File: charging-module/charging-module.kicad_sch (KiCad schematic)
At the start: 12 parts, among them J1 Bat, U1 MCP73833-xxx-UN

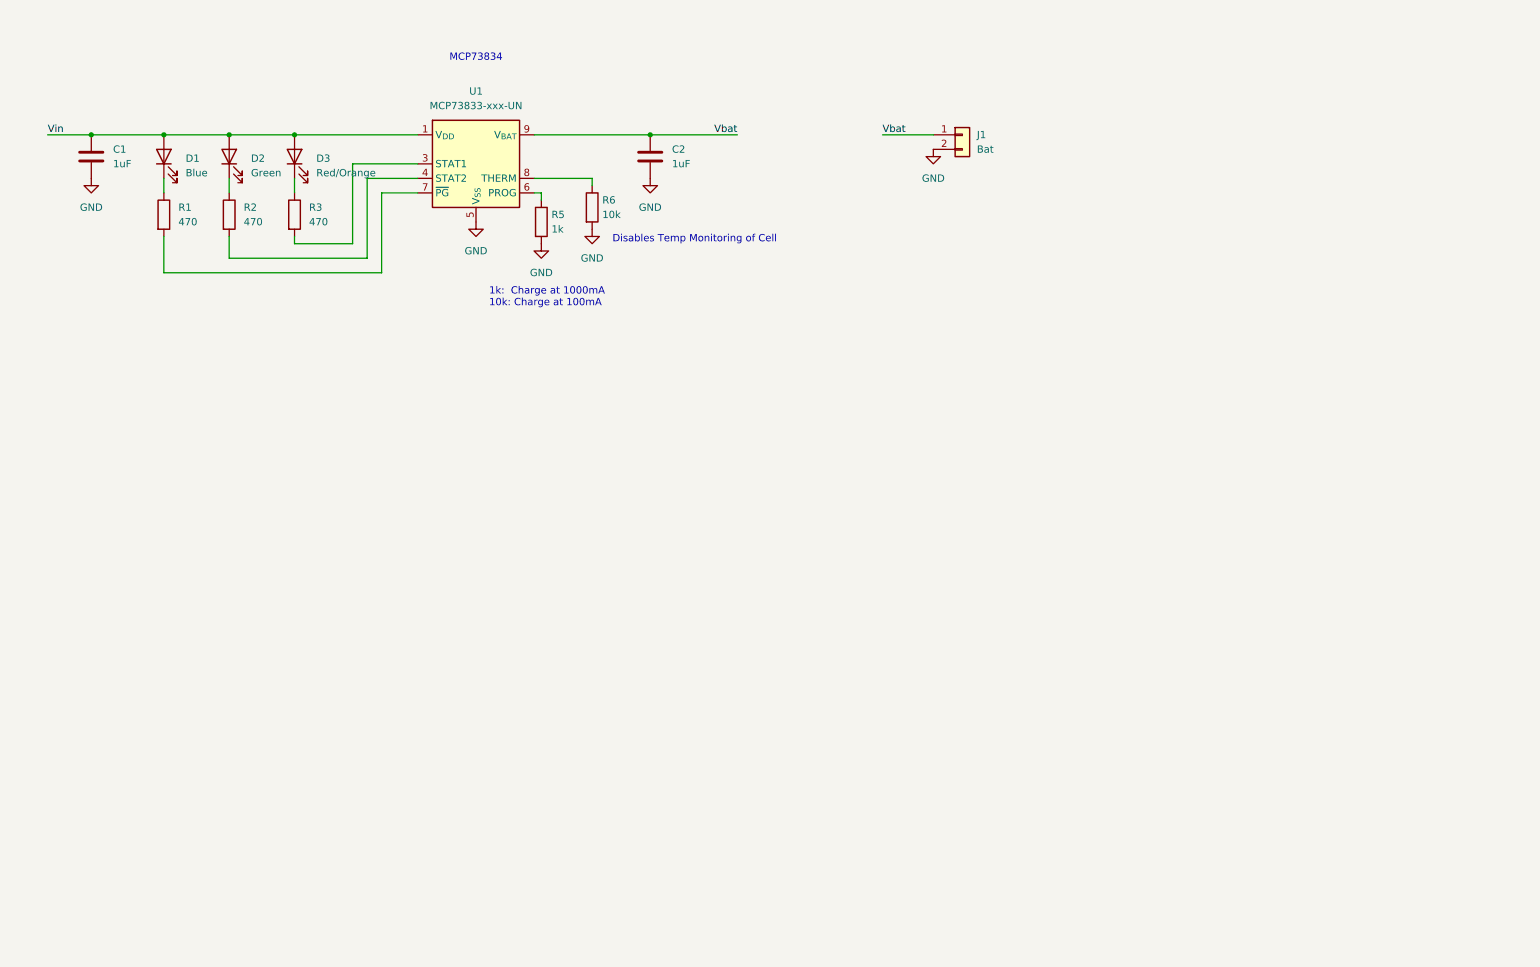
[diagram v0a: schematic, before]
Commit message: MCP73871 schematic
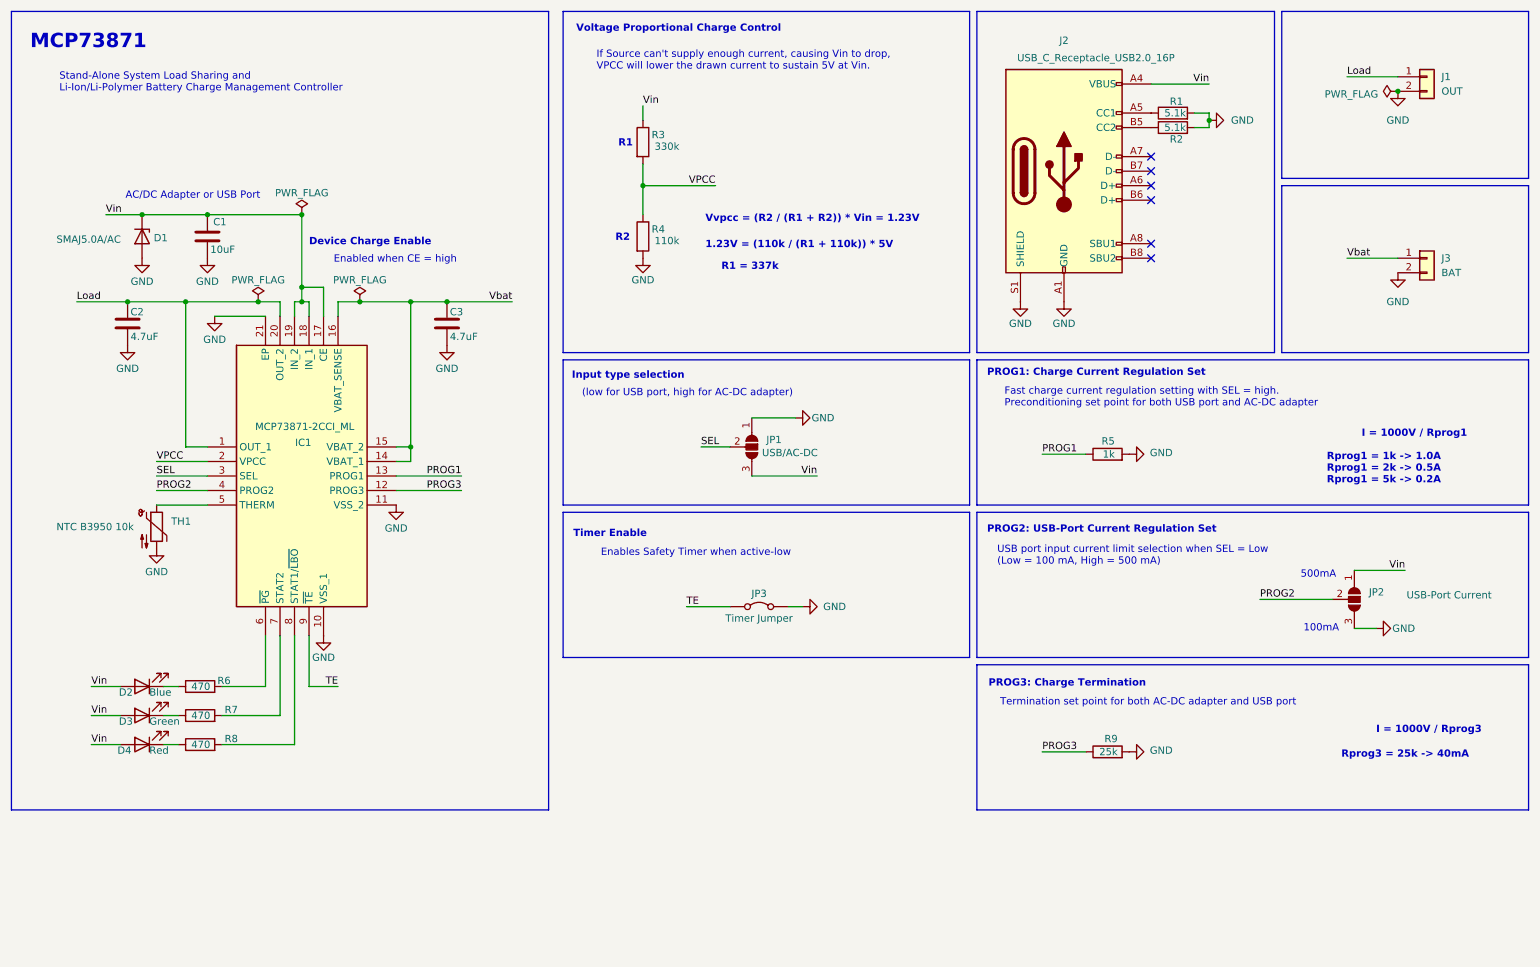
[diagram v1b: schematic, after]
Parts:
- removed D1: Blue, symbol Device:LED
- removed U1: MCP73833-xxx-UN, Package_SO:MSOP-10_3x3mm_P0.5mm, symbol Battery_Management:MCP73833-xxx-UN
- added C3: 4.7uF, symbol Device:C
- added D1: SMAJ5.0A/AC, symbol Device:D_Zener
- added D4: Red, symbol Device:LED
- added IC1: MCP73871-2CCI_ML, MCP73871-2CCI_ML:QFN50P400X400X100-21N-D, symbol MCP73871-2CCI_ML:MCP73871-2CCI_ML
- added J1: OUT, Connector_JST:JST_XH_S2B-XH-A_1x02_P2.50mm_Horizontal, symbol Connector_Generic:Conn_01x02
- added J2: USB_C_Receptacle_USB2.0_16P, Connector_USB:USB_C_Receptacle_HRO_TYPE-C-31-M-12, symbol Connector:USB_C_Receptacle_USB2.0_16P
- added JP1: USB/AC-DC, Connector_PinHeader_2.54mm:PinHeader_1x03_P2.54mm_Horizontal, symbol Jumper:SolderJumper_3_Open
- added JP2: USB-Port Current, Jumper:SolderJumper-3_P1.3mm_Bridged12_RoundedPad1.0x1.5mm_NumberLabels, symbol Jumper:SolderJumper_3_Open
- added JP3: Timer Jumper, Jumper:SolderJumper-2_P1.3mm_Bridged_RoundedPad1.0x1.5mm, symbol Jumper:Jumper_2_Bridged
- added R4: 110k, symbol Device:R
- added R7, R8: 470, symbol Device:R
- added R9: 25k, symbol Device:R
- added TH1: NTC B3950 10k, Connector_PinHeader_1.00mm:PinHeader_1x02_P1.00mm_Vertical, symbol Device:Thermistor_NTC
- C1: value 1uF -> 10uF
- C2: value 1uF -> 4.7uF
- D2: value Green -> Blue
- D3: value Red/Orange -> Green
- J3: renamed from J1; value Bat -> BAT; footprint (none) -> Connector_JST:JST_XH_S2B-XH-A_1x02_P2.50mm_Horizontal
- R1, R2: value 470 -> 5.1k
- R3: value 470 -> 330k
- R6: value 10k -> 470
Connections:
- net GND: now also R1.2, R2.2, C3.2, D1.2 (A), IC1.10 (VSS_1), IC1.11 (VSS_2), IC1.21 (EP), J1.2 (Pin_2), J2.A1 (GND), J2.A12 (GND), J2.B1 (GND), J2.B12 (GND), J2.S1 (SHIELD), JP1.1 (A), JP2.3 (B), JP3.2 (B), R4.2, R9.2, TH1.2; no longer R6.2
- net Vbat: now also C3.1, IC1.14 (VBAT_1), IC1.15 (VBAT_2), IC1.16 (VBAT_SENSE); no longer C2.1
- net Vin: now also R3.1, D1.1 (K), D4.2 (A), IC1.17 (CE), IC1.18 (IN_1), IC1.19 (IN_2), J2.A4 (VBUS), J2.A9 (VBUS), J2.B4 (VBUS), J2.B9 (VBUS), JP1.3 (B), JP2.1 (A)
- net at R1.1: now also J2.A5 (CC1)
- net at D2.1 (K): now also R6.1; no longer R2.1
- net PROG1: now reaches R5.1
- net PROG1: now also IC1.13 (PROG1)
- net at D3.1 (K): now also R7.1; no longer R3.1
- net VPCC: now reaches R3.2
- net VPCC: now also IC1.2 (VPCC), R4.1
- new net: IC1.5 (THERM), TH1.1
- new net: IC1.7 (STAT2), R7.2
- new net: IC1.6 (~{PG}), R6.2
- new net: IC1.8 (STAT1/~{LBO}), R8.2
- new net: J2.B5 (CC2), R2.1
- new net: D4.1 (K), R8.1
- new net Load: C2.1, IC1.1 (OUT_1), IC1.20 (OUT_2), J1.1 (Pin_1)
- new net PROG2: IC1.4 (PROG2), JP2.2 (C)
- new net PROG3: IC1.12 (PROG3), R9.1
- new net SEL: IC1.3 (SEL), JP1.2 (C)
- new net TE: IC1.9 (~{TE}), JP3.1 (A)
- no-connect marks 0 -> 6
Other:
- note added: "(low for USB port, high for AC-DC adapter)"
- note added: "1.23V = (110k / (R1 + 110k)) * 5V"
- note added: "100mA"
- note added: "500mA"
- note added: "AC/DC Adapter or USB Port"
- note added: "Device Charge Enable"
- note added: "Enabled when CE = high"
- note added: "Enables Safety Timer when active-low"
- note added: "Fast charge current regulation setting with SEL = high. Preconditioning set point for both USB port and AC-DC adapter"
- note added: "I = 1000V / Rprog1"
- note added: "I = 1000V / Rprog3"
- note added: "If Source can't supply enough current, causing Vin to drop, VPCC will lower the drawn current to sustain 5V at Vin."
- note added: "Input type selection"
- note added: "MCP73871"
- note added: "PROG1: Charge Current Regulation Set"
- note added: "PROG2: USB-Port Current Regulation Set"
- note added: "PROG3: Charge Termination"
- note added: "R1"
- note added: "R1 = 337k"
- note added: "R2"
- note added: "Rprog1 = 1k -> 1.0A"
- note added: "Rprog1 = 2k -> 0.5A"
- note added: "Rprog1 = 5k -> 0.2A"
- note added: "Rprog3 = 25k -> 40mA"
- note added: "Stand-Alone System Load Sharing and Li-Ion/Li-Polymer Battery Charge Management Controller"
- note added: "Termination set point for both AC-DC adapter and USB port"
- note added: "Timer Enable"
- note added: "USB port input current limit selection when SEL = Low (Low = 100 mA, High = 500 mA)"
- note added: "Voltage Proportional Charge Control"
- note added: "Vvpcc = (R2 / (R1 + R2)) * Vin = 1.23V"
- note removed: "1k: Charge at 1000mA 10k: Charge at 100mA"
- note removed: "Disables Temp Monitoring of Cell"
- note removed: "MCP73834"
- moved on the sheet: J3

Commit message: removed overvoltage diode
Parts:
- removed D1: SMAJ5.0A/AC, symbol Device:D_Zener
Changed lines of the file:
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@@
 	)
 	(junction
-		(at 40.64 49.53)
-		(diameter 0)
-		(color 0 0 0 0)
-	)
-	(junction
 		(at 38.1 64.77)
 		(diameter 0)
@@
 	(wire
 		(pts
-			(xy 40.64 49.53) (xy 52.07 49.53)
-		)
-		(stroke
-			(width 0)
-			(type default)
-		)
-	)
-	(wire
-		(pts
 			(xy 62.23 132.08) (xy 62.23 123.19)
 		)
@@
 	(wire
 		(pts
-			(xy 34.29 49.53) (xy 40.64 49.53)
+			(xy 34.29 49.53) (xy 52.07 49.53)
 		)
 		(stroke
@@
 	(symbol
 		(lib_id "power:GND")
-		(at 40.64 57.15 0)
-		(unit 1)
-		(exclude_from_sim no)
-		(in_bom yes)
-		(on_board yes)
-		(dnp no)
-		(property "Reference" "#PWR03"
-			(at 40.64 63.5 0)
-			(effects
-				(font
-					(size 1.27 1.27)
-				)
-				(hide yes)
-			)
-		)
-		(property "Value" "GND"
-			(at 40.64 61.214 0)
-			(effects
-				(font
-					(size 1.27 1.27)
-				)
-			)
-		)
-		(property "Footprint" ""
-			(at 40.64 57.15 0)
-			(effects
-				(font
-					(size 1.27 1.27)
-				)
-				(hide yes)
-			)
-		)
-		(property "Datasheet" ""
-			(at 40.64 57.15 0)
-			(effects
-				(font
-					(size 1.27 1.27)
-				)
-				(hide yes)
-			)
-		)
-		(property "Description" "Power symbol creates a global label with name \"GND\" , ground"
-			(at 40.64 57.15 0)
-			(effects
-				(font
-					(size 1.27 1.27)
-				)
-				(hide yes)
-			)
-		)
-		(pin "1"
-		)
-		(instances
-			(project "charging-module"
-				(path "/81b77902-7571-4357-bdb3-0a0c14837efb"
-					(reference "#PWR03")
-					(unit 1)
-				)
-			)
-		)
-	)
-	(symbol
-		(lib_id "power:GND")
 		(at 53.34 67.31 0)
 		(unit 1)
@@
 					(unit 1)
 				)
-			)
-		)
-	)
-	(symbol
-		(lib_id "Device:D_Zener")
-		(at 40.64 53.34 270)
-		(unit 1)
-		(exclude_from_sim no)
-		(in_bom yes)
-		(on_board yes)
-		(dnp no)
-		(property "Reference" "D1"
-			(at 42.672 53.594 90)
-			(effects
-				(font
-					(size 1.27 1.27)
-				)
-				(justify left)
-			)
-		)
-		(property "Value" "SMAJ5.0A/AC"
-			(at 25.654 53.848 90)
-			(effects
-				(font
-					(size 1.27 1.27)
-				)
-				(justify left)
-			)
-		)
-		(property "Footprint" ""
-			(at 40.64 53.34 0)
-			(effects
-				(font
-					(size 1.27 1.27)
-				)
-				(hide yes)
-			)
-		)
-		(property "Datasheet" "~"
-			(at 40.64 53.34 0)
-			(effects
-				(font
-					(size 1.27 1.27)
-				)
-				(hide yes)
-			)
-		)
-		(property "Description" "Zener diode"
-			(at 40.64 53.34 0)
-			(effects
-				(font
-					(size 1.27 1.27)
-				)
-				(hide yes)
-			)
-		)
-		(pin "2"
-		)
-		(pin "1"
-		)
-		(instances
-			(project ""
-				(path "/81b77902-7571-4357-bdb3-0a0c14837efb"
-					(reference "D1")
-					(unit 1)
-				)

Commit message: assigned footprints
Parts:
- C1, C2, C3: footprint (none) -> Capacitor_SMD:C_0805_2012Metric_Pad1.18x1.45mm_HandSolder
- D2, D3, D4: footprint (none) -> LED_SMD:LED_0805_2012Metric_Pad1.15x1.40mm_HandSolder
- R1, R2, R3, R4, R5, R6, R7, R8, R9: footprint (none) -> Resistor_SMD:R_0805_2012Metric_Pad1.20x1.40mm_HandSolder
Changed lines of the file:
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@@
 			)
 		)
-		(property "Footprint" ""
+		(property "Footprint" "Resistor_SMD:R_0805_2012Metric_Pad1.20x1.40mm_HandSolder"
 			(at 50.8 138.938 90)
 			(effects
@@
 			)
 		)
-		(property "Footprint" ""
+		(property "Footprint" "Capacitor_SMD:C_0805_2012Metric_Pad1.18x1.45mm_HandSolder"
 			(at 94.9452 72.39 0)
 			(effects
@@
 			)
 		)
-		(property "Footprint" ""
+		(property "Footprint" "Capacitor_SMD:C_0805_2012Metric_Pad1.18x1.45mm_HandSolder"
 			(at 53.0352 57.15 0)
 			(effects
@@
 			)
 		)
-		(property "Footprint" ""
+		(property "Footprint" "LED_SMD:LED_0805_2012Metric_Pad1.15x1.40mm_HandSolder"
 			(at 40.64 132.08 0)
 			(effects
@@
 			)
 		)
-		(property "Footprint" ""
+		(property "Footprint" "LED_SMD:LED_0805_2012Metric_Pad1.15x1.40mm_HandSolder"
 			(at 40.64 137.16 0)
 			(effects
@@
 			)
 		)
-		(property "Footprint" ""
+		(property "Footprint" "Resistor_SMD:R_0805_2012Metric_Pad1.20x1.40mm_HandSolder"
 			(at 50.8 144.018 90)
 			(effects
@@
 			)
 		)
-		(property "Footprint" ""
+		(property "Footprint" "Capacitor_SMD:C_0805_2012Metric_Pad1.18x1.45mm_HandSolder"
 			(at 39.0652 72.39 0)
 			(effects
@@
 			)
 		)
-		(property "Footprint" ""
+		(property "Footprint" "Resistor_SMD:R_0805_2012Metric_Pad1.20x1.40mm_HandSolder"
 			(at 126.492 36.83 90)
 			(effects
@@
 			)
 		)
-		(property "Footprint" ""
+		(property "Footprint" "Resistor_SMD:R_0805_2012Metric_Pad1.20x1.40mm_HandSolder"
 			(at 220.98 36.068 90)
 			(effects
@@
 			)
 		)
-		(property "Footprint" ""
+		(property "Footprint" "Resistor_SMD:R_0805_2012Metric_Pad1.20x1.40mm_HandSolder"
 			(at 50.8 133.858 90)
 			(effects
@@
 			)
 		)
-		(property "Footprint" ""
+		(property "Footprint" "Resistor_SMD:R_0805_2012Metric_Pad1.20x1.40mm_HandSolder"
 			(at 209.55 93.218 90)
 			(effects
@@
 			)
 		)
-		(property "Footprint" ""
+		(property "Footprint" "Resistor_SMD:R_0805_2012Metric_Pad1.20x1.40mm_HandSolder"
 			(at 220.98 33.528 90)
 			(effects
@@
 			)
 		)
-		(property "Footprint" ""
+		(property "Footprint" "Resistor_SMD:R_0805_2012Metric_Pad1.20x1.40mm_HandSolder"
 			(at 209.55 145.288 90)
 			(effects
@@
 			)
 		)
-		(property "Footprint" ""
+		(property "Footprint" "LED_SMD:LED_0805_2012Metric_Pad1.15x1.40mm_HandSolder"
 			(at 40.64 142.24 0)
 			(effects
@@
 			)
 		)
-		(property "Footprint" ""
+		(property "Footprint" "Resistor_SMD:R_0805_2012Metric_Pad1.20x1.40mm_HandSolder"
 			(at 126.492 53.34 90)
 			(effects

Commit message: started on layout
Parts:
- TH1: footprint Connector_PinHeader_1.00mm:PinHeader_1x02_P1.00mm_Vertical -> Connector_PinHeader_2.54mm:PinHeader_1x02_P2.54mm_Vertical
- renumbered D2 to D1, D3 to D2, D4 to D3
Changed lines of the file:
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@@
 			)
 		)
-		(property "Footprint" "Connector_PinHeader_1.00mm:PinHeader_1x02_P1.00mm_Vertical"
+		(property "Footprint" "Connector_PinHeader_2.54mm:PinHeader_1x02_P2.54mm_Vertical"
 			(at 43.18 102.87 0)
 			(effects
@@
 		(on_board yes)
 		(dnp no)
-		(property "Reference" "#PWR013"
+		(property "Reference" "#PWR012"
 			(at 219.71 91.44 0)
 			(effects
@@
 			(project "charging-module"
 				(path "/81b77902-7571-4357-bdb3-0a0c14837efb"
-					(reference "#PWR013")
+					(reference "#PWR012")
 					(unit 1)
 				)
@@
 		(on_board yes)
 		(dnp no)
-		(property "Reference" "#PWR09"
+		(property "Reference" "#PWR08"
 			(at 53.34 73.66 0)
 			(effects
@@
 			(project "charging-module"
 				(path "/81b77902-7571-4357-bdb3-0a0c14837efb"
-					(reference "#PWR09")
+					(reference "#PWR08")
 					(unit 1)
 				)
@@
 		(on_board yes)
 		(dnp no)
-		(property "Reference" "#PWR012"
+		(property "Reference" "#PWR011"
 			(at 161.29 85.09 0)
 			(effects
@@
 			(project "charging-module"
 				(path "/81b77902-7571-4357-bdb3-0a0c14837efb"
-					(reference "#PWR012")
+					(reference "#PWR011")
 					(unit 1)
 				)
@@
 		(on_board yes)
 		(dnp no)
-		(property "Reference" "#PWR011"
+		(property "Reference" "#PWR010"
 			(at 93.98 78.74 0)
 			(effects
@@
 			(project "charging-module"
 				(path "/81b77902-7571-4357-bdb3-0a0c14837efb"
-					(reference "#PWR011")
+					(reference "#PWR010")
 					(unit 1)
 				)
@@
 		(on_board yes)
 		(dnp no)
-		(property "Reference" "#PWR015"
+		(property "Reference" "#PWR014"
 			(at 43.18 114.3 0)
 			(effects
@@
 			(project "charging-module"
 				(path "/81b77902-7571-4357-bdb3-0a0c14837efb"
-					(reference "#PWR015")
+					(reference "#PWR014")
 					(unit 1)
 				)
@@
 		(on_board yes)
 		(dnp no)
-		(property "Reference" "#PWR08"
+		(property "Reference" "#PWR07"
 			(at 201.93 71.12 0)
 			(effects
@@
 			(project "charging-module"
 				(path "/81b77902-7571-4357-bdb3-0a0c14837efb"
-					(reference "#PWR08")
+					(reference "#PWR07")
 					(unit 1)
 				)
@@
 		(on_board yes)
 		(dnp no)
-		(property "Reference" "#PWR019"
+		(property "Reference" "#PWR015"
 			(at 162.56 118.11 0)
 			(effects
@@
 			(project "charging-module"
 				(path "/81b77902-7571-4357-bdb3-0a0c14837efb"
-					(reference "#PWR019")
+					(reference "#PWR015")
 					(unit 1)
 				)
@@
 		(on_board yes)
 		(dnp no)
-		(property "Reference" "D2"
+		(property "Reference" "D1"
 			(at 36.576 133.096 0)
 			(effects
@@
 			(project "charging-module"
 				(path "/81b77902-7571-4357-bdb3-0a0c14837efb"
-					(reference "D2")
+					(reference "D1")
 					(unit 1)
 				)
@@
 		(on_board yes)
 		(dnp no)
-		(property "Reference" "#PWR014"
+		(property "Reference" "#PWR013"
 			(at 85.09 106.68 0)
 			(effects
@@
 			(project "charging-module"
 				(path "/81b77902-7571-4357-bdb3-0a0c14837efb"
-					(reference "#PWR014")
+					(reference "#PWR013")
 					(unit 1)
 				)
@@
 		(on_board yes)
 		(dnp no)
-		(property "Reference" "#FLG02"
+		(property "Reference" "#FLG03"
 			(at 60.96 62.865 0)
 			(effects
@@
 			(project "charging-module"
 				(path "/81b77902-7571-4357-bdb3-0a0c14837efb"
-					(reference "#FLG02")
+					(reference "#FLG03")
 					(unit 1)
 				)
@@
 		(on_board yes)
 		(dnp no)
-		(property "Reference" "#FLG01"
+		(property "Reference" "#FLG02"
 			(at 68.58 47.625 0)
 			(effects
@@
 			(project ""
 				(path "/81b77902-7571-4357-bdb3-0a0c14837efb"
-					(reference "#FLG01")
+					(reference "#FLG02")
 					(unit 1)
 				)
@@
 		(on_board yes)
 		(dnp no)
-		(property "Reference" "D3"
+		(property "Reference" "D2"
 			(at 36.576 138.176 0)
 			(effects
@@
 			(project "charging-module"
 				(path "/81b77902-7571-4357-bdb3-0a0c14837efb"
-					(reference "D3")
+					(reference "D2")
 					(unit 1)
 				)
@@
 		(on_board yes)
 		(dnp no)
-		(property "Reference" "#FLG03"
+		(property "Reference" "#FLG04"
 			(at 78.74 62.865 0)
 			(effects
@@
 			(project "charging-module"
 				(path "/81b77902-7571-4357-bdb3-0a0c14837efb"
-					(reference "#FLG03")
+					(reference "#FLG04")
 					(unit 1)
 				)
@@
 		(on_board yes)
 		(dnp no)
-		(property "Reference" "#PWR010"
+		(property "Reference" "#PWR09"
 			(at 38.1 78.74 0)
 			(effects
@@
 			(project "charging-module"
 				(path "/81b77902-7571-4357-bdb3-0a0c14837efb"
-					(reference "#PWR010")
+					(reference "#PWR09")
 					(unit 1)
 				)
@@
 		(on_board yes)
 		(dnp no)
-		(property "Reference" "#PWR04"
+		(property "Reference" "#PWR03"
 			(at 52.07 63.5 0)
 			(effects
@@
 			(project "charging-module"
 				(path "/81b77902-7571-4357-bdb3-0a0c14837efb"
-					(reference "#PWR04")
+					(reference "#PWR03")
 					(unit 1)
 				)
@@
 		(on_board yes)
 		(dnp no)
-		(property "Reference" "#PWR05"
+		(property "Reference" "#PWR04"
 			(at 128.27 63.5 0)
 			(effects
@@
 			(project "charging-module"
 				(path "/81b77902-7571-4357-bdb3-0a0c14837efb"
-					(reference "#PWR05")
+					(reference "#PWR04")
 					(unit 1)
 				)
@@
 		(on_board yes)
 		(dnp no)
-		(property "Reference" "#PWR07"
+		(property "Reference" "#PWR06"
 			(at 194.31 71.12 0)
 			(effects
@@
 			(project "charging-module"
 				(path "/81b77902-7571-4357-bdb3-0a0c14837efb"
-					(reference "#PWR07")
+					(reference "#PWR06")
 					(unit 1)
 				)
@@
 		(on_board yes)
 		(dnp no)
-		(property "Reference" "#FLG04"
+		(property "Reference" "#FLG01"
 			(at 258.445 27.94 0)
 			(effects
@@
 			(project "charging-module"
 				(path "/81b77902-7571-4357-bdb3-0a0c14837efb"
-					(reference "#FLG04")
+					(reference "#FLG01")
 					(unit 1)
 				)
@@
 		(dnp no)
 		(fields_autoplaced yes)
-		(property "Reference" "#PWR06"
+		(property "Reference" "#PWR05"
 			(at 260.35 66.04 0)
 			(effects
@@
 			(project "charging-module"
 				(path "/81b77902-7571-4357-bdb3-0a0c14837efb"
-					(reference "#PWR06")
+					(reference "#PWR05")
 					(unit 1)
 				)
@@
 		(on_board yes)
 		(dnp no)
-		(property "Reference" "D4"
+		(property "Reference" "D3"
 			(at 36.322 143.256 0)
 			(effects
@@
 			(project "charging-module"
 				(path "/81b77902-7571-4357-bdb3-0a0c14837efb"
-					(reference "D4")
-					(unit 1)
-				)
+					(reference "D3")
+					(unit 1)
+				)

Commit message: layout
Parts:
- added H1, H2, H3: MountingHole_Pad, MountingHole:MountingHole_2.2mm_M2_DIN965_Pad, symbol Mechanical:MountingHole_Pad
- JP1: footprint Connector_PinHeader_2.54mm:PinHeader_1x03_P2.54mm_Horizontal -> Connector_PinHeader_2.54mm:PinHeader_1x03_P2.54mm_Vertical
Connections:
- net GND: now also H1.1, H2.1, H3.1
